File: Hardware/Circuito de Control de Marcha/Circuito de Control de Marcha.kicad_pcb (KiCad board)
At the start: 2 copper layers, 42 parts, among them Q1 IRF9540N, Q1A1 2N2219, Q2 IRF540N, Q2A1 2N2219, Q3 IRF9540N, Q3A1 2N2219, Q4 IRF540N, Q4A1 2N2219, Q5 IRF9540N, Q5A1 2N2219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

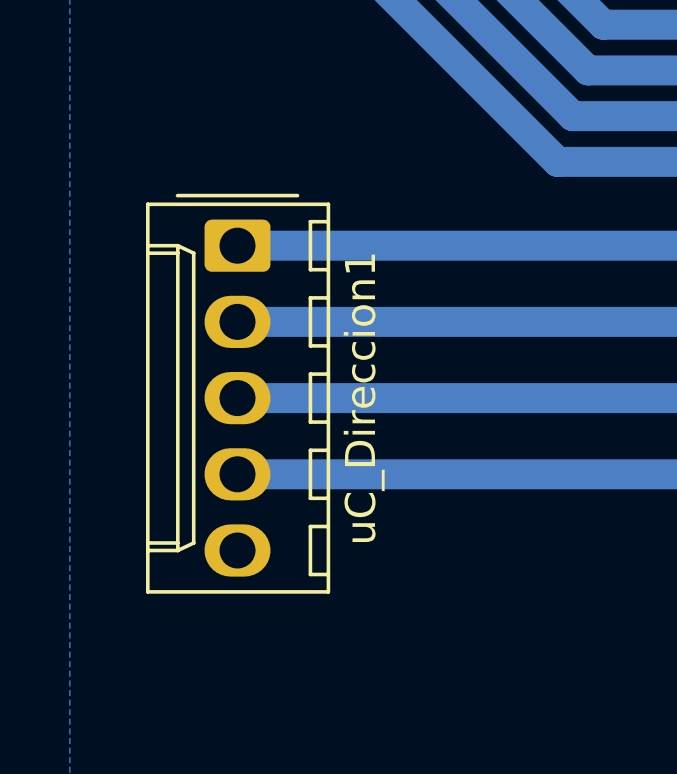
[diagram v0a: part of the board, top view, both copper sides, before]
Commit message: Correxion en el control de marcha
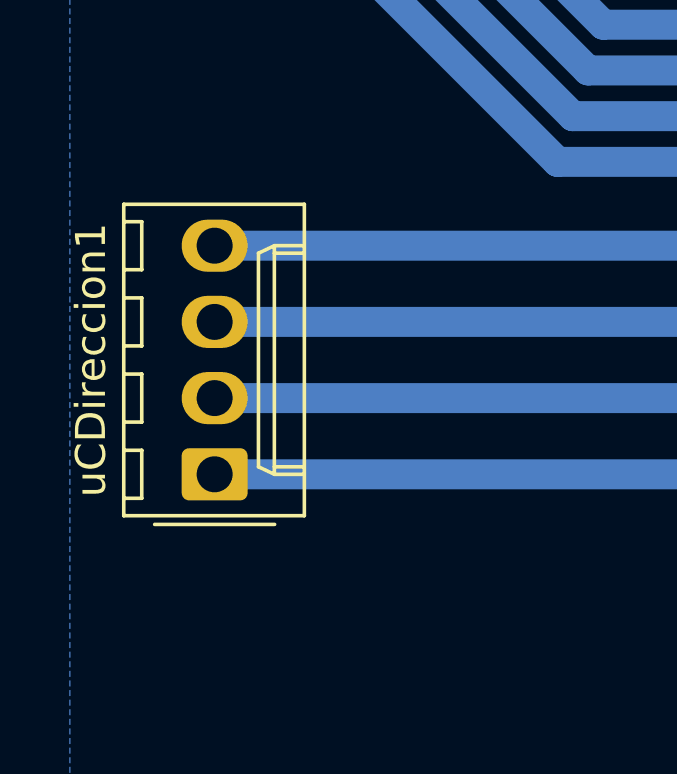
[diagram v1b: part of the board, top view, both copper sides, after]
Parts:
- removed uC_Direccion1: Screw_Terminal_01x05, Connector_Molex:Molex_KK-254_AE-6410-05A_1x05_P2.54mm_Vertical
- added uCDireccion1: Screw_Terminal_01x04, Connector_Molex:Molex_KK-254_AE-6410-04A_1x04_P2.54mm_Vertical, F.Cu at (110.2, 128.0)
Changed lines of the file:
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@@
     (add_net "Net-(U1-Pad7)")
+  )
+  (module Connector_Molex:Molex_KK-254_AE-6410-04A_1x04_P2.54mm_Vertical (layer F.Cu)
+    (at 110.236 128.016 90)
+    (descr "Molex KK-254 Interconnect System, old/engineering part number: AE-6410-04A example for new part number: 22-27-2041, 4 Pins (http://www.molex.com/pdm_docs/sd/022272021_sd.pdf), generated with kicad-footprint-generator")
+    (tags "connector Molex KK-254 side entry")
+    (fp_text reference uCDireccion1 (at 3.81 -4.12 90) (layer F.SilkS)
+      (effects (font (size 1 1) (thickness 0.15)))
+    )
+    (fp_text value Screw_Terminal_01x04 (at 3.81 4.08 90) (layer F.Fab)
+      (effects (font (size 1 1) (thickness 0.15)))
+    )
+    (fp_text user %R (at 3.81 -2.22 90) (layer F.Fab)
+      (effects (font (size 1 1) (thickness 0.15)))
+    )
+    (fp_line (start 9.39 -3.42) (end -1.77 -3.42) (layer F.CrtYd) (width 0.05))
+    (fp_line (start 9.39 3.38) (end 9.39 -3.42) (layer F.CrtYd) (width 0.05))
+    (fp_line (start -1.77 3.38) (end 9.39 3.38) (layer F.CrtYd) (width 0.05))
+    (fp_line (start -1.77 -3.42) (end -1.77 3.38) (layer F.CrtYd) (width 0.05))
+    (fp_line (start 8.42 -2.43) (end 8.42 -3.03) (layer F.SilkS) (width 0.12))
+    (fp_line (start 6.82 -2.43) (end 8.42 -2.43) (layer F.SilkS) (width 0.12))
+    (fp_line (start 6.82 -3.03) (end 6.82 -2.43) (layer F.SilkS) (width 0.12))
+    (fp_line (start 5.88 -2.43) (end 5.88 -3.03) (layer F.SilkS) (width 0.12))
+    (fp_line (start 4.28 -2.43) (end 5.88 -2.43) (layer F.SilkS) (width 0.12))
+    (fp_line (start 4.28 -3.03) (end 4.28 -2.43) (layer F.SilkS) (width 0.12))
+    (fp_line (start 3.34 -2.43) (end 3.34 -3.03) (layer F.SilkS) (width 0.12))
+    (fp_line (start 1.74 -2.43) (end 3.34 -2.43) (layer F.SilkS) (width 0.12))
+    (fp_line (start 1.74 -3.03) (end 1.74 -2.43) (layer F.SilkS) (width 0.12))
+    (fp_line (start 0.8 -2.43) (end 0.8 -3.03) (layer F.SilkS) (width 0.12))
+    (fp_line (start -0.8 -2.43) (end 0.8 -2.43) (layer F.SilkS) (width 0.12))
+    (fp_line (start -0.8 -3.03) (end -0.8 -2.43) (layer F.SilkS) (width 0.12))
+    (fp_line (start 7.37 2.99) (end 7.37 1.99) (layer F.SilkS) (width 0.12))
+    (fp_line (start 0.25 2.99) (end 0.25 1.99) (layer F.SilkS) (width 0.12))
+    (fp_line (start 7.37 1.46) (end 7.62 1.99) (layer F.SilkS) (width 0.12))
+    (fp_line (start 0.25 1.46) (end 7.37 1.46) (layer F.SilkS) (width 0.12))
+    (fp_line (start 0 1.99) (end 0.25 1.46) (layer F.SilkS) (width 0.12))
+    (fp_line (start 7.62 1.99) (end 7.62 2.99) (layer F.SilkS) (width 0.12))
+    (fp_line (start 0 1.99) (end 7.62 1.99) (layer F.SilkS) (width 0.12))
+    (fp_line (start 0 2.99) (end 0 1.99) (layer F.SilkS) (width 0.12))
+    (fp_line (start -0.562893 0) (end -1.27 0.5) (layer F.Fab) (width 0.1))
+    (fp_line (start -1.27 -0.5) (end -0.562893 0) (layer F.Fab) (width 0.1))
+    (fp_line (start -1.67 -2) (end -1.67 2) (layer F.SilkS) (width 0.12))
+    (fp_line (start 9 -3.03) (end -1.38 -3.03) (layer F.SilkS) (width 0.12))
+    (fp_line (start 9 2.99) (end 9 -3.03) (layer F.SilkS) (width 0.12))
+    (fp_line (start -1.38 2.99) (end 9 2.99) (layer F.SilkS) (width 0.12))
+    (fp_line (start -1.38 -3.03) (end -1.38 2.99) (layer F.SilkS) (width 0.12))
+    (fp_line (start 8.89 -2.92) (end -1.27 -2.92) (layer F.Fab) (width 0.1))
+    (fp_line (start 8.89 2.88) (end 8.89 -2.92) (layer F.Fab) (width 0.1))
+    (fp_line (start -1.27 2.88) (end 8.89 2.88) (layer F.Fab) (width 0.1))
+    (fp_line (start -1.27 -2.92) (end -1.27 2.88) (layer F.Fab) (width 0.1))
+    (pad 4 thru_hole oval (at 7.62 0 90) (size 1.74 2.2) (drill 1.2) (layers *.Cu *.Mask)
+      (net 35 "Net-(U1-Pad1)"))
+    (pad 3 thru_hole oval (at 5.08 0 90) (size 1.74 2.2) (drill 1.2) (layers *.Cu *.Mask)
+      (net 34 "Net-(U1-Pad2)"))
+    (pad 2 thru_hole oval (at 2.54 0 90) (size 1.74 2.2) (drill 1.2) (layers *.Cu *.Mask)
+      (net 33 "Net-(U1-Pad3)"))
+    (pad 1 thru_hole roundrect (at 0 0 90) (size 1.74 2.2) (drill 1.2) (layers *.Cu *.Mask) (roundrect_rratio 0.143678)
+      (net 31 "Net-(U1-Pad4)"))
+    (model ${KISYS3DMOD}/Connector_Molex.3dshapes/Molex_KK-254_AE-6410-04A_1x04_P2.54mm_Vertical.wrl
+      (at (xyz 0 0 0))
+      (scale (xyz 1 1 1))
+      (rotate (xyz 0 0 0))
+    )
   )
   (module Capacitor_THT:C_Disc_D4.3mm_W1.9mm_P5.00mm (layer F.Cu)
@@
       (at (xyz 0 0 0))
       (scale (xyz 1 1 1))
-      (rotate (xyz 0 0 0))
-    )
-  )
-  (module Connector_Molex:Molex_KK-254_AE-6410-05A_1x05_P2.54mm_Vertical (layer F.Cu)
-    (at 110.998 120.396 270)
-    (descr "Molex KK-254 Interconnect System, old/engineering part number: AE-6410-05A example for new part number: 22-27-2051, 5 Pins (http://www.molex.com/pdm_docs/sd/022272021_sd.pdf), generated with kicad-footprint-generator")
-    (tags "connector Molex KK-254 side entry")
-    (fp_text reference uC_Direccion1 (at 5.08 -4.12 90) (layer F.SilkS)
-      (effects (font (size 1 1) (thickness 0.15)))
-    )
-    (fp_text value Screw_Terminal_01x05 (at 5.08 4.08 90) (layer F.Fab)
-      (effects (font (size 1 1) (thickness 0.15)))
-    )
-    (fp_text user %R (at 5.08 -2.22 90) (layer F.Fab)
-      (effects (font (size 1 1) (thickness 0.15)))
-    )
-    (fp_line (start 11.93 -3.42) (end -1.77 -3.42) (layer F.CrtYd) (width 0.05))
-    (fp_line (start 11.93 3.38) (end 11.93 -3.42) (layer F.CrtYd) (width 0.05))
-    (fp_line (start -1.77 3.38) (end 11.93 3.38) (layer F.CrtYd) (width 0.05))
-    (fp_line (start -1.77 -3.42) (end -1.77 3.38) (layer F.CrtYd) (width 0.05))
-    (fp_line (start 10.96 -2.43) (end 10.96 -3.03) (layer F.SilkS) (width 0.12))
-    (fp_line (start 9.36 -2.43) (end 10.96 -2.43) (layer F.SilkS) (width 0.12))
-    (fp_line (start 9.36 -3.03) (end 9.36 -2.43) (layer F.SilkS) (width 0.12))
-    (fp_line (start 8.42 -2.43) (end 8.42 -3.03) (layer F.SilkS) (width 0.12))
-    (fp_line (start 6.82 -2.43) (end 8.42 -2.43) (layer F.SilkS) (width 0.12))
-    (fp_line (start 6.82 -3.03) (end 6.82 -2.43) (layer F.SilkS) (width 0.12))
-    (fp_line (start 5.88 -2.43) (end 5.88 -3.03) (layer F.SilkS) (width 0.12))
-    (fp_line (start 4.28 -2.43) (end 5.88 -2.43) (layer F.SilkS) (width 0.12))
-    (fp_line (start 4.28 -3.03) (end 4.28 -2.43) (layer F.SilkS) (width 0.12))
-    (fp_line (start 3.34 -2.43) (end 3.34 -3.03) (layer F.SilkS) (width 0.12))
-    (fp_line (start 1.74 -2.43) (end 3.34 -2.43) (layer F.SilkS) (width 0.12))
-    (fp_line (start 1.74 -3.03) (end 1.74 -2.43) (layer F.SilkS) (width 0.12))
-    (fp_line (start 0.8 -2.43) (end 0.8 -3.03) (layer F.SilkS) (width 0.12))
-    (fp_line (start -0.8 -2.43) (end 0.8 -2.43) (layer F.SilkS) (width 0.12))
-    (fp_line (start -0.8 -3.03) (end -0.8 -2.43) (layer F.SilkS) (width 0.12))
-    (fp_line (start 9.91 2.99) (end 9.91 1.99) (layer F.SilkS) (width 0.12))
-    (fp_line (start 0.25 2.99) (end 0.25 1.99) (layer F.SilkS) (width 0.12))
-    (fp_line (start 9.91 1.46) (end 10.16 1.99) (layer F.SilkS) (width 0.12))
-    (fp_line (start 0.25 1.46) (end 9.91 1.46) (layer F.SilkS) (width 0.12))
-    (fp_line (start 0 1.99) (end 0.25 1.46) (layer F.SilkS) (width 0.12))
-    (fp_line (start 10.16 1.99) (end 10.16 2.99) (layer F.SilkS) (width 0.12))
-    (fp_line (start 0 1.99) (end 10.16 1.99) (layer F.SilkS) (width 0.12))
-    (fp_line (start 0 2.99) (end 0 1.99) (layer F.SilkS) (width 0.12))
-    (fp_line (start -0.562893 0) (end -1.27 0.5) (layer F.Fab) (width 0.1))
-    (fp_line (start -1.27 -0.5) (end -0.562893 0) (layer F.Fab) (width 0.1))
-    (fp_line (start -1.67 -2) (end -1.67 2) (layer F.SilkS) (width 0.12))
-    (fp_line (start 11.54 -3.03) (end -1.38 -3.03) (layer F.SilkS) (width 0.12))
-    (fp_line (start 11.54 2.99) (end 11.54 -3.03) (layer F.SilkS) (width 0.12))
-    (fp_line (start -1.38 2.99) (end 11.54 2.99) (layer F.SilkS) (width 0.12))
-    (fp_line (start -1.38 -3.03) (end -1.38 2.99) (layer F.SilkS) (width 0.12))
-    (fp_line (start 11.43 -2.92) (end -1.27 -2.92) (layer F.Fab) (width 0.1))
-    (fp_line (start 11.43 2.88) (end 11.43 -2.92) (layer F.Fab) (width 0.1))
-    (fp_line (start -1.27 2.88) (end 11.43 2.88) (layer F.Fab) (width 0.1))
-    (fp_line (start -1.27 -2.92) (end -1.27 2.88) (layer F.Fab) (width 0.1))
-    (pad 5 thru_hole oval (at 10.16 0 270) (size 1.74 2.2) (drill 1.2) (layers *.Cu *.Mask)
-      (net 10 Earth))
-    (pad 4 thru_hole oval (at 7.62 0 270) (size 1.74 2.2) (drill 1.2) (layers *.Cu *.Mask)
-      (net 31 "Net-(U1-Pad4)"))
-    (pad 3 thru_hole oval (at 5.08 0 270) (size 1.74 2.2) (drill 1.2) (layers *.Cu *.Mask)
-      (net 33 "Net-(U1-Pad3)"))
-    (pad 2 thru_hole oval (at 2.54 0 270) (size 1.74 2.2) (drill 1.2) (layers *.Cu *.Mask)
-      (net 34 "Net-(U1-Pad2)"))
-    (pad 1 thru_hole roundrect (at 0 0 270) (size 1.74 2.2) (drill 1.2) (layers *.Cu *.Mask) (roundrect_rratio 0.143678)
-      (net 35 "Net-(U1-Pad1)"))
-    (model ${KISYS3DMOD}/Connector_Molex.3dshapes/Molex_KK-254_AE-6410-05A_1x05_P2.54mm_Vertical.wrl
-      (at (xyz 0 0 0))
-      (scale (xyz 1 1 1))

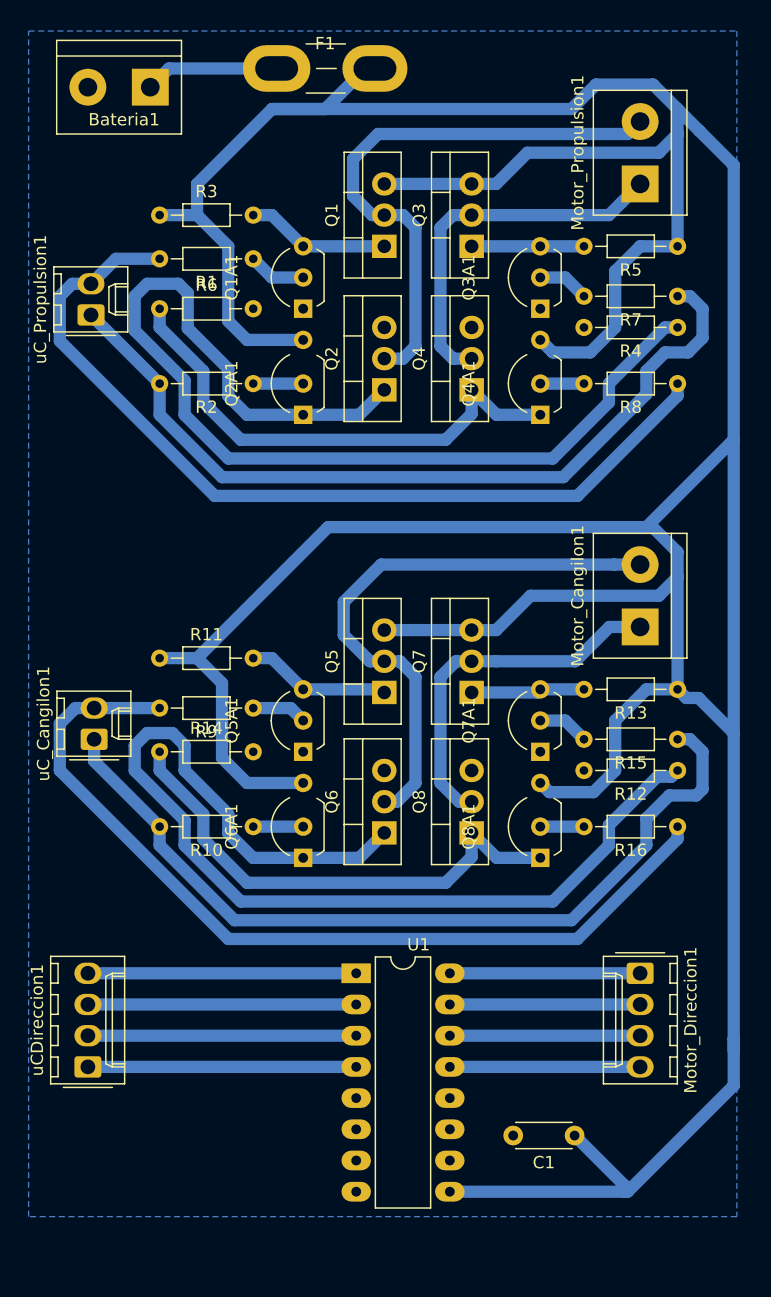
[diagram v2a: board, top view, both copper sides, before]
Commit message: PCB control de marcha
Intente hacer el PCB pero me queda una conexion de los púentes H
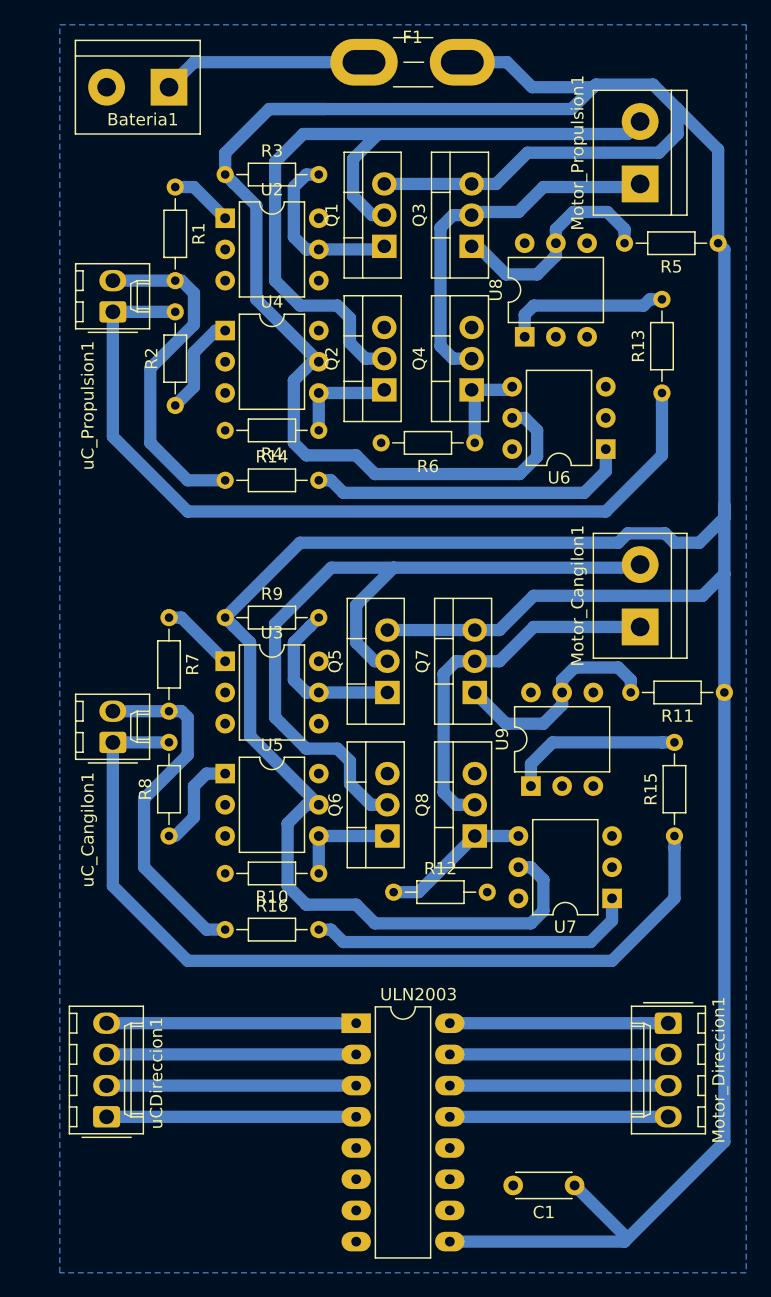
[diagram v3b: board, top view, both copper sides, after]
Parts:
- removed Q1A1, Q2A1, Q3A1, Q4A1, Q5A1, Q6A1, Q7A1, Q8A1: 2N2219, Package_TO_SOT_THT:TO-92L_Inline_Wide
- added U2: 4N25, Package_DIP:DIP-6_W7.62mm, F.Cu at (121.4, 58.9)
- added U3: 4N25, Package_DIP:DIP-6_W7.62mm, F.Cu at (121.4, 95.0)
- added U4: 4N25, Package_DIP:DIP-6_W7.62mm, F.Cu at (121.4, 68.1)
- added U5: 4N25, Package_DIP:DIP-6_W7.62mm, F.Cu at (121.4, 104.1)
- added U6: 4N25, Package_DIP:DIP-6_W7.62mm, F.Cu at (152.4, 77.7)
- added U7: 4N25, Package_DIP:DIP-6_W7.62mm, F.Cu at (152.9, 114.3)
- added U8: 4N25, Package_DIP:DIP-6_W7.62mm, F.Cu at (145.8, 68.6)
- added U9: 4N25, Package_DIP:DIP-6_W7.62mm, F.Cu at (146.3, 105.2)
- R1, R13, R14, R15, R16, R2, R7, R8: value R -> 220
- R10, R11, R12, R3, R4, R5, R6, R9: value R -> 10k
- moved R8 55.4 mm to (116.8, 109.2), turned to 90 degrees
- moved R7 49.0 mm to (116.8, 91.4), turned to 270 degrees
- moved R11 46.1 mm to (162.1, 97.5), turned to 180 degrees
- moved R16 37.8 mm to (121.4, 116.8), turned to 0 degrees
- moved R4 30.4 mm to (129.0, 76.2)
- moved R6 27.9 mm to (141.7, 77.2), turned to 180 degrees
- moved R12 25.1 mm to (135.1, 113.8), turned to 0 degrees
- moved R13 24.2 mm to (157.0, 73.2), turned to 90 degrees
- moved R14 22.7 mm to (121.4, 80.3)
- moved R1 8.63 mm to (117.3, 56.4), turned to 270 degrees
- moved R15 7.88 mm to (158.0, 109.2), turned to 90 degrees
- moved R9 7.71 mm to (121.4, 91.4), turned to 0 degrees
- moved F1 7.13 mm to (132.7, 46.2)
- moved R2 6.59 mm to (117.3, 74.2), turned to 90 degrees
- moved R10 6.55 mm to (129.0, 112.3)
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- renumbered U1 to ULN2003
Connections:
- R10 pad 1: Net-(Q6A1-Pad2) -> Net-(Q6-Pad1)
- R10 pad 2: Net-(R10-Pad2) -> Earth
- R11 pad 2: Net-(Q5-Pad1) -> Net-(Q7-Pad1)
- R12 pad 1: Net-(Q6-Pad1) -> Net-(Q8-Pad1)
- R13 pad 1: Net-(C1-Pad1) -> Net-(R13-Pad1)
- R13 pad 2: Net-(Q7-Pad1) -> Net-(R13-Pad2)
- R14 pad 1: Net-(Q8-Pad1) -> Net-(R1-Pad2)
- R14 pad 2: Earth -> Net-(R14-Pad2)
- R15 pad 1: Net-(R10-Pad2) -> Net-(R15-Pad1)
- R2 pad 2: Net-(R2-Pad2) -> Net-(R13-Pad1)
- R7 pad 1: Net-(R2-Pad2) -> Net-(R7-Pad1)
- R7 pad 2: Net-(Q3A1-Pad2) -> Net-(R16-Pad1)
- R8 pad 1: Net-(R1-Pad2) -> Net-(R8-Pad1)
- R8 pad 2: Net-(Q4A1-Pad2) -> Net-(R15-Pad1)
- R9 pad 1: Net-(Q5A1-Pad2) -> Net-(C1-Pad1)
- R9 pad 2: Net-(R16-Pad1) -> Net-(Q5-Pad1)
- uC_Cangilon1 pad 1: Net-(R10-Pad2) -> Net-(R15-Pad1)
- uC_Propulsion1 pad 1: Net-(R2-Pad2) -> Net-(R13-Pad1)
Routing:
- net Net-(Q2-Pad1): track 87.2 -> 8.49 mm
- net Net-(Q6-Pad1): track 85.1 -> 8.64 mm
- net Net-(R15-Pad1): track 0.00 -> 71.7 mm
- net Net-(R13-Pad1): track 0.00 -> 69.4 mm
- net Net-(R10-Pad2): track 68.8 -> 0.00 mm
- net Net-(R2-Pad2): track 67.4 -> 0.00 mm
- net Net-(R1-Pad2): track 72.9 -> 28.0 mm
- net Net-(R16-Pad1): track 72.8 -> 28.7 mm
- net Net-(Q4-Pad1): track 41.5 -> 7.83 mm
- net Net-(Q8-Pad1): track 41.2 -> 12.1 mm
- net Net-(R14-Pad2): track 0.00 -> 26.3 mm
- net Net-(R16-Pad2): track 3.56 -> 26.8 mm
- net Net-(Motor_Propulsion1-Pad2): track 46.4 -> 62.5 mm
- net Net-(Motor_Cangilon1-Pad2): track 47.1 -> 63.0 mm
- net Net-(R13-Pad2): track 0.00 -> 13.5 mm
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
